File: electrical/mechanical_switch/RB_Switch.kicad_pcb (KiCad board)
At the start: 4 copper layers, 115 x 38 mm, 33 parts, among them SW1 SW_TH_Tactile_Omron_B3F-10xx, SW2 SW_TH_Tactile_Omron_B3F-10xx, SW3 SW_TH_Tactile_Omron_B3F-10xx, U1 ESP32-S2-MINI-1

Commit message: Address DRC shorts and minimum-clearance congestion
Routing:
- net USB_CC2: track 47.3 -> 43.2 mm, vias 2 -> 1
- net USB_DP: track 85.4 -> 84.8 mm, vias 3 -> 1
- net USB_DM: track 86.1 -> 85.6 mm, vias 3 -> 1
- net USB_CC1: vias 2 -> 1
- net VBAT: vias 6 -> 5
- net GND: vias 54 -> 44

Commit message: Re-route crowded PCB signal corridors and regulator connections
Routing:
- net SW1_NET: track 105.3 -> 103.3 mm
- net USB_DP: track 84.8 -> 83.1 mm
- net USB_DM: track 85.6 -> 83.8 mm, vias 1 -> 0
- net SW2_NET: track 96.3 -> 95.0 mm
- net USB_CC1: track 45.8 -> 45.0 mm
- net VBAT: vias 5 -> 4
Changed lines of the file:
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@@
-	)
-	(segment
-		(start 87.75 97.75)
-		(end 87 97.75)
-		(width 0.2)
-		(layer "In1.Cu")
-		(net "USB_CC1")
 	)
 	(segment
@@
 	)
 	(via
-		(at 105.4 87)
-		(size 0.5)
-		(drill 0.3)
-		(layers "F.Cu" "B.Cu")
-		(covering
-			(front no)
-			(back no)
-		)
-		(net "VBAT")
-	)
-	(via
 		(at 121.225 86)
 		(size 0.5)
@@
 	)
 	(segment
-		(start 124.75 99)
-		(end 124.75 99.5)
-		(width 0.2)
-		(layer "In2.Cu")
-		(net "SW1_NET")
-	)
-	(segment
 		(start 156.25 100.25)
 		(end 156.25 104)
@@
 	)
 	(segment
-		(start 125.5 100)
-		(end 125.5 100.25)
-		(width 0.2)
-		(layer "In2.Cu")
-		(net "SW1_NET")
-	)
-	(segment
-		(start 124.75 99.5)
-		(end 125 99.5)
-		(width 0.2)
-		(layer "In2.Cu")
-		(net "SW1_NET")
-	)
-	(segment
 		(start 156.5 104.5)
 		(end 157 104.5)
@@
 	)
 	(segment
-		(start 125 100)
-		(end 125.5 100)
-		(width 0.2)
-		(layer "In2.Cu")
-		(net "SW1_NET")
-	)
-	(segment
 		(start 165.5 112.25)
 		(end 171.25 112.25)
@@
 	)
 	(segment
-		(start 125 99.5)
-		(end 125 100)
-		(width 0.2)
-		(layer "In2.Cu")
-		(net "SW1_NET")
-	)
-	(segment
 		(start 165.5 112.5)
 		(end 165.5 112.25)
@@
 	)
 	(segment
-		(start 150 98.5)
-		(end 150 98)
-		(width 0.2)
-		(layer "In2.Cu")
-		(net "SW2_NET")
-	)
-	(segment
 		(start 163.225 113)
 		(end 164.25 113)
@@
 	)
 	(segment
-		(start 149.75 99)
-		(end 149.75 98.5)
-		(width 0.2)
-		(layer "In2.Cu")
-		(net "SW2_NET")
-	)
-	(segment
 		(start 172 92.5)
 		(end 171.75 92.5)
@@
 		(net "SW2_NET")
 	)
-	(segment
-		(start 149.75 98.5)
-		(end 150 98.5)
-		(width 0.2)
-		(layer "In2.Cu")
-		(net "SW2_NET")
-	)
 	(via
 		(at 169.45 93.05)
@@
 		(net "SW3_NET")
 	)
-	(via
-		(at 169.45 99)
-		(size 0.5)
-		(drill 0.3)
-		(layers "F.Cu" "B.Cu")
-		(covering
-			(front no)
-			(back no)
-		)
-		(net "USB_DM")
-	)
-	(segment
-		(start 99.75 98.75)
-		(end 99.75 98.5)
-		(width 0.2)
-		(layer "In1.Cu")
-		(net "USB_DM")
-	)
-	(segment
-		(start 100 98)
-		(end 100.5 98)
-		(width 0.2)
-		(layer "In1.Cu")
-		(net "USB_DM")
-	)
 	(segment
 		(start 88.25 98.75)
@@
 	)
 	(segment
-		(start 100.5 98)
-		(end 100.5 97.75)
-		(width 0.2)
-		(layer "In1.Cu")
-		(net "USB_DM")
-	)
-	(segment
 		(start 87.68 98.75)
 		(end 99.75 98.75)
@@
 	)
 	(segment
-		(start 99.75 98.5)
-		(end 100 98.5)
-		(width 0.2)
-		(layer "In1.Cu")
-		(net "USB_DM")
-	)
-	(segment
-		(start 100 98.5)
-		(end 100 98)
-		(width 0.2)
-		(layer "In1.Cu")
-		(net "USB_DM")
-	)
-	(segment
 		(start 169.5 97.75)
 		(end 169.5 99)
@@
 	)
 	(segment
-		(start 99.75 99.5)
-		(end 100 99.5)
-		(width 0.2)
-		(layer "B.Cu")
-		(net "USB_DP")
-	)
-	(segment
 		(start 87.68 99.25)
 		(end 99.75 99.25)
@@
 	)
 	(segment
-		(start 99.75 99.25)
-		(end 99.75 99.5)
-		(width 0.2)
-		(layer "B.Cu")
-		(net "USB_DP")
-	)
-	(segment
-		(start 100 99.5)
-		(end 100 100)
-		(width 0.2)
-		(layer "B.Cu")
-		(net "USB_DP")
-	)
-	(segment
-		(start 100.5 100)
-		(end 100.5 100.25)
-		(width 0.2)
-		(layer "B.Cu")
-		(net "USB_DP")
-	)
-	(segment
 		(start 88.25 99.25)
 		(end 87.75 99.25)
@@
 		(start 88.25 98.25)
 		(end 88.25 99.25)
-		(width 0.2)
-		(layer "B.Cu")
-		(net "USB_DP")
-	)
-	(segment
-		(start 100 100)
-		(end 100.5 100)
 		(width 0.2)
 		(layer "B.Cu")
@@
 		(layer "B.Cu")
 		(net "L_A")
-	)
+	)\n\t(segment\n\t\t(start 87.68 97.75)\n\t\t(end 87.75 97.75)\n\t\t(width 0.2)\n\t\t(layer "In1.Cu")\n\t\t(net "USB_CC1")\n\t\t\n\t)\n\t(segment\n\t\t(start 99.75 99.25)\n\t\t(end 99.75 100.25)\n\t\t(width 0.2)\n\t\t(layer "B.Cu")\n\t\t(net "USB_DP")\n\t\t\n\t)\n\t(segment\n\t\t(start 99.75 100.25)\n\t\t(end 100.5 100.25)\n\t\t(width 0.2)\n\t\t(layer "B.Cu")\n\t\t(net "USB_DP")\n\t\t\n\t)\n\t(segment\n\t\t(start 99.75 98.75)\n\t\t(end 99.75 97.75)\n\t\t(width 0.2)\n\t\t(layer "In1.Cu")\n\t\t(net "USB_DM")\n\t\t\n\t)\n\t(segment\n\t\t(start 99.75 97.75)\n\t\t(end 100.5 97.75)\n\t\t(width 0.2)\n\t\t(layer "In1.Cu")\n\t\t(net "USB_DM")\n\t\t\n\t)\n\t(segment\n\t\t(start 124.75 99)\n\t\t(end 124.75 101)\n\t\t(width 0.2)\n\t\t(layer "In2.Cu")\n\t\t(net "SW1_NET")\n\t\t\n\t)\n\t(segment\n\t\t(start 124.75 101)\n\t\t(end 125.5 101)\n\t\t(width 0.2)\n\t\t(layer "In2.Cu")\n\t\t(net "SW1_NET")\n\t\t\n\t)\n\t(segment\n\t\t(start 125.5 101)\n\t\t(end 125.5 100.25)\n\t\t(width 0.2)\n\t\t(layer "In2.Cu")\n\t\t(net "SW1_NET")\n\t\t\n\t)\n\t(segment\n\t\t(start 149.75 99)\n\t\t(end 149.75 97.75)\n\t\t(width 0.2)\n\t\t(layer "In2.Cu")\n\t\t(net "SW2_NET")\n\t\t\n\t)\n\t(segment\n\t\t(start 149.75 97.75)\n\t\t(end 150.5 97.75)\n\t\t(width 0.2)\n\t\t(layer "In2.Cu")\n\t\t(net "SW2_NET")\n\t\t\n\t)\n\t(segment\n\t\t(start 150.5 97.75)\n\t\t(end 150.5 98)\n\t\t(width 0.2)\n\t\t(layer "In2.Cu")\n\t\t(net "SW2_NET")\n\t\t\n\t)\n\t(segment\n\t\t(start 150.5 98)\n\t\t(end 150 98)\n\t\t(width 0.2)\n\t\t(layer "In2.Cu")\n\t\t(net "SW2_NET")\n\t\t\n\t)\n\t(segment\n\t\t(start 102.6 85.5)\n\t\t(end 101 84.5)\n\t\t(width 0.2)\n\t\t(layer "F.Cu")\n\t\t(net "L_B")\n\t\t\n\t)\n\t(segment\n\t\t(start 102.6 86.5)\n\t\t(end 101 87.5)\n\t\t(width 0.2)\n\t\t(layer "F.Cu")\n\t\t(net "L_A")\n\t\t\n\t)\n\t(segment\n\t\t(start 102.6 85)\n\t\t(end 101 83.5)\n\t\t(width 0.2)\n\t\t(layer "F.Cu")\n\t\t(net "V3V3")\n\t\t\n\t)\n\t(segment\n\t\t(start 102.6 87)\n\t\t(end 103.5 88.5)\n\t\t(width 0.2)\n\t\t(layer "F.Cu")\n\t\t(net "VBAT")\n\t\t\n\t)\n\t(segment\n\t\t(start 102.6 86)\n\t\t(end 103.425 86)\n\t\t(width 0.2)\n\t\t(layer "F.Cu")\n\t\t(net "GND")\n\t\t\n\t)\n\t(segment\n\t\t(start 105.4 85.5)\n\t\t(end 104.575 86)\n\t\t(width 0.2)\n\t\t(layer "F.Cu")\n\t\t(net "GND")\n\t\t\n\t)\n\t(segment\n\t\t(start 105.4 86.5)\n\t\t(end 104.575 86)\n\t\t(width 0.2)\n\t\t(layer "F.Cu")\n\t\t(net "GND")\n\t\t\n\t)\n\t(segment\n\t\t(start 87.68 100.75)\n\t\t(end 88.25 100.75)\n\t\t(width 0.2)\n\t\t(layer "F.Cu")\n\t\t(net "USB_CC2")\n\t\t\n\t)

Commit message: Repair PCB routing changes and keep board syntax valid
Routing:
- net SW1_NET: track 103.3 -> 106.8 mm
- net GND: track 0.00 -> 2.75 mm
- net SW2_NET: track 95.0 -> 97.8 mm
- net V3V3: track 0.00 -> 2.19 mm
- net L_B: track 5.00 -> 6.89 mm
- net L_A: track 5.00 -> 6.89 mm
- net USB_DP: track 83.1 -> 84.8 mm
- net USB_DM: track 83.8 -> 85.6 mm
- net VBAT: track 73.6 -> 75.4 mm
- net USB_CC2: track 43.2 -> 43.8 mm
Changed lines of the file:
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@@
 	)
 	(embedded_fonts no)
-)
-	(via
-		(at 90 97)
-		(size 0.5)
-		(drill 0.3)
-		(layers "F.Cu" "B.Cu")
-		(net "USB_CC1")
-	)
-	(via
-		(at 90 98)
-		(size 0.5)
-		(drill 0.3)
-		(layers "F.Cu" "B.Cu")
-		(net "USB_DP")
-	)
-	(via
-		(at 90 99)
-		(size 0.5)
-		(drill 0.3)
-		(layers "F.Cu" "B.Cu")
-		(net "USB_DP")
-	)
-	(via
-		(at 91 98.5)
-		(size 0.5)
-		(drill 0.3)
-		(layers "F.Cu" "B.Cu")
-		(net "USB_DM")
-	)
-	(via
-		(at 91 99.5)
-		(size 0.5)
-		(drill 0.3)
-		(layers "F.Cu" "B.Cu")
-		(net "USB_DM")
-	)
-	(via
-		(at 91 100.5)
-		(size 0.5)
-		(drill 0.3)
-		(layers "F.Cu" "B.Cu")
-		(net "USB_CC2")
-	)
 	(segment
-		(start 90 97)
+		(start 87.68 97.75)
 		(end 87.75 97.75)
 		(width 0.2)
@@
 	)
 	(segment
-		(start 90 98)
-		(end 88.25 98.25)
+		(start 99.75 99.25)
+		(end 99.75 100.25)
 		(width 0.2)
 		(layer "B.Cu")
@@
 	)
 	(segment
-		(start 90 99)
-		(end 88.25 99.25)
+		(start 99.75 100.25)
+		(end 100.5 100.25)
 		(width 0.2)
 		(layer "B.Cu")
@@
 	)
 	(segment
-		(start 91 98.5)
-		(end 88.25 98.75)
+		(start 99.75 98.75)
+		(end 99.75 97.75)
 		(width 0.2)
 		(layer "In1.Cu")
@@
 	)
 	(segment
-		(start 91 99.5)
-		(end 88.25 99.75)
+		(start 99.75 97.75)
+		(end 100.5 97.75)
 		(width 0.2)
 		(layer "In1.Cu")
@@
 	)
 	(segment
-		(start 91 100.5)
-		(end 91.75 100.75)
+		(start 124.75 99)
+		(end 124.75 101)
 		(width 0.2)
-		(layer "B.Cu")
-		(net "USB_CC2")
+		(layer "In2.Cu")
+		(net "SW1_NET")
 	)
 	(segment
-		(start 101 84.5)
-		(end 101 85.25)
+		(start 124.75 101)
+		(end 125.5 101)
 		(width 0.2)
-		(layer "B.Cu")
+		(layer "In2.Cu")
+		(net "SW1_NET")
+	)
+	(segment
+		(start 125.5 101)
+		(end 125.5 100.25)
+		(width 0.2)
+		(layer "In2.Cu")
+		(net "SW1_NET")
+	)
+	(segment
+		(start 149.75 99)
+		(end 149.75 97.75)
+		(width 0.2)
+		(layer "In2.Cu")
+		(net "SW2_NET")
+	)
+	(segment
+		(start 149.75 97.75)
+		(end 150.5 97.75)
+		(width 0.2)
+		(layer "In2.Cu")
+		(net "SW2_NET")
+	)
+	(segment
+		(start 150.5 97.75)
+		(end 150.5 98)
+		(width 0.2)
+		(layer "In2.Cu")
+		(net "SW2_NET")
+	)
+	(segment
+		(start 150.5 98)
+		(end 150 98)
+		(width 0.2)
+		(layer "In2.Cu")
+		(net "SW2_NET")
+	)
+	(segment
+		(start 102.6 85.5)
+		(end 101 84.5)
+		(width 0.2)
+		(layer "F.Cu")
 		(net "L_B")
 	)
 	(segment
-		(start 101 84.5)
-		(end 98.5 84.5)
+		(start 102.6 86.5)
+		(end 101 87.5)
 		(width 0.2)
-		(layer "B.Cu")
-		(net "L_B")
-	)
-	(segment
-		(start 101 87.5)
-		(end 102 87.5)
-		(width 0.2)
-		(layer "B.Cu")
+		(layer "F.Cu")
 		(net "L_A")
 	)
 	(segment
-		(start 101 87.5)
-		(end 98.5 87.5)
-		(width 0.2)
-		(layer "B.Cu")
-		(net "L_A")
-	)
-	(segment
-		(start 101 83.5)
-		(end 102.6 85)
+		(start 102.6 85)
+		(end 101 83.5)
 		(width 0.2)
 		(layer "F.Cu")
@@
 	)
 	(segment
-		(start 103.5 88.5)
-		(end 103.5 87.5)
+		(start 102.6 87)
+		(end 103.5 88.5)
 		(width 0.2)
-		(layer "B.Cu")
+		(layer "F.Cu")
 		(net "VBAT")
 	)
 	(segment
-		(start 98.6 83.725)
-		(end 98.5 84.5)
+		(start 102.6 86)
+		(end 103.425 86)
 		(width 0.2)
-		(layer "B.Cu")
-		(net "L_B")
+		(layer "F.Cu")
+		(net "GND")
 	)
 	(segment
-		(start 98.6 88.275)
-		(end 98.5 87.5)
+		(start 105.4 85.5)
+		(end 104.575 86)
 		(width 0.2)
-		(layer "B.Cu")
-		(net "L_A")
-	)\n\t(segment\n\t\t(start 87.68 97.75)\n\t\t(end 87.75 97.75)\n\t\t(width 0.2)\n\t\t(layer "In1.Cu")\n\t\t(net "USB_CC1")\n\t\t\n\t)\n\t(segment\n\t\t(start 99.75 99.25)\n\t\t(end 99.75 100.25)\n\t\t(width 0.2)\n\t\t(layer "B.Cu")\n\t\t(net "USB_DP")\n\t\t\n\t)\n\t(segment\n\t\t(start 99.75 100.25)\n\t\t(end 100.5 100.25)\n\t\t(width 0.2)\n\t\t(layer "B.Cu")\n\t\t(net "USB_DP")\n\t\t\n\t)\n\t(segment\n\t\t(start 99.75 98.75)\n\t\t(end 99.75 97.75)\n\t\t(width 0.2)\n\t\t(layer "In1.Cu")\n\t\t(net "USB_DM")\n\t\t\n\t)\n\t(segment\n\t\t(start 99.75 97.75)\n\t\t(end 100.5 97.75)\n\t\t(width 0.2)\n\t\t(layer "In1.Cu")\n\t\t(net "USB_DM")\n\t\t\n\t)\n\t(segment\n\t\t(start 124.75 99)\n\t\t(end 124.75 101)\n\t\t(width 0.2)\n\t\t(layer "In2.Cu")\n\t\t(net "SW1_NET")\n\t\t\n\t)\n\t(segment\n\t\t(start 124.75 101)\n\t\t(end 125.5 101)\n\t\t(width 0.2)\n\t\t(layer "In2.Cu")\n\t\t(net "SW1_NET")\n\t\t\n\t)\n\t(segment\n\t\t(start 125.5 101)\n\t\t(end 125.5 100.25)\n\t\t(width 0.2)\n\t\t(layer "In2.Cu")\n\t\t(net "SW1_NET")\n\t\t\n\t)\n\t(segment\n\t\t(start 149.75 99)\n\t\t(end 149.75 97.75)\n\t\t(width 0.2)\n\t\t(layer "In2.Cu")\n\t\t(net "SW2_NET")\n\t\t\n\t)\n\t(segment\n\t\t(start 149.75 97.75)\n\t\t(end 150.5 97.75)\n\t\t(width 0.2)\n\t\t(layer "In2.Cu")\n\t\t(net "SW2_NET")\n\t\t\n\t)\n\t(segment\n\t\t(start 150.5 97.75)\n\t\t(end 150.5 98)\n\t\t(width 0.2)\n\t\t(layer "In2.Cu")\n\t\t(net "SW2_NET")\n\t\t\n\t)\n\t(segment\n\t\t(start 150.5 98)\n\t\t(end 150 98)\n\t\t(width 0.2)\n\t\t(layer "In2.Cu")\n\t\t(net "SW2_NET")\n\t\t\n\t)\n\t(segment\n\t\t(start 102.6 85.5)\n\t\t(end 101 84.5)\n\t\t(width 0.2)\n\t\t(layer "F.Cu")\n\t\t(net "L_B")\n\t\t\n\t)\n\t(segment\n\t\t(start 102.6 86.5)\n\t\t(end 101 87.5)\n\t\t(width 0.2)\n\t\t(layer "F.Cu")\n\t\t(net "L_A")\n\t\t\n\t)\n\t(segment\n\t\t(start 102.6 85)\n\t\t(end 101 83.5)\n\t\t(width 0.2)\n\t\t(layer "F.Cu")\n\t\t(net "V3V3")\n\t\t\n\t)\n\t(segment\n\t\t(start 102.6 87)\n\t\t(end 103.5 88.5)\n\t\t(width 0.2)\n\t\t(layer "F.Cu")\n\t\t(net "VBAT")\n\t\t\n\t)\n\t(segment\n\t\t(start 102.6 86)\n\t\t(end 103.425 86)\n\t\t(width 0.2)\n\t\t(layer "F.Cu")\n\t\t(net "GND")\n\t\t\n\t)\n\t(segment\n\t\t(start 105.4 85.5)\n\t\t(end 104.575 86)\n\t\t(width 0.2)\n\t\t(layer "F.Cu")\n\t\t(net "GND")\n\t\t\n\t)\n\t(segment\n\t\t(start 105.4 86.5)\n\t\t(end 104.575 86)\n\t\t(width 0.2)\n\t\t(layer "F.Cu")\n\t\t(net "GND")\n\t\t\n\t)\n\t(segment\n\t\t(start 87.68 100.75)\n\t\t(end 88.25 100.75)\n\t\t(width 0.2)\n\t\t(layer "F.Cu")\n\t\t(net "USB_CC2")\n\t\t\n\t)
+		(layer "F.Cu")
+		(net "GND")
+	)
+	(segment
+		(start 105.4 86.5)
+		(end 104.575 86)
+		(width 0.2)
+		(layer "F.Cu")
+		(net "GND")
+	)
+	(segment
+		(start 87.68 100.75)
+		(end 88.25 100.75)
+		(width 0.2)
+		(layer "F.Cu")
+		(net "USB_CC2")
+	)
+)

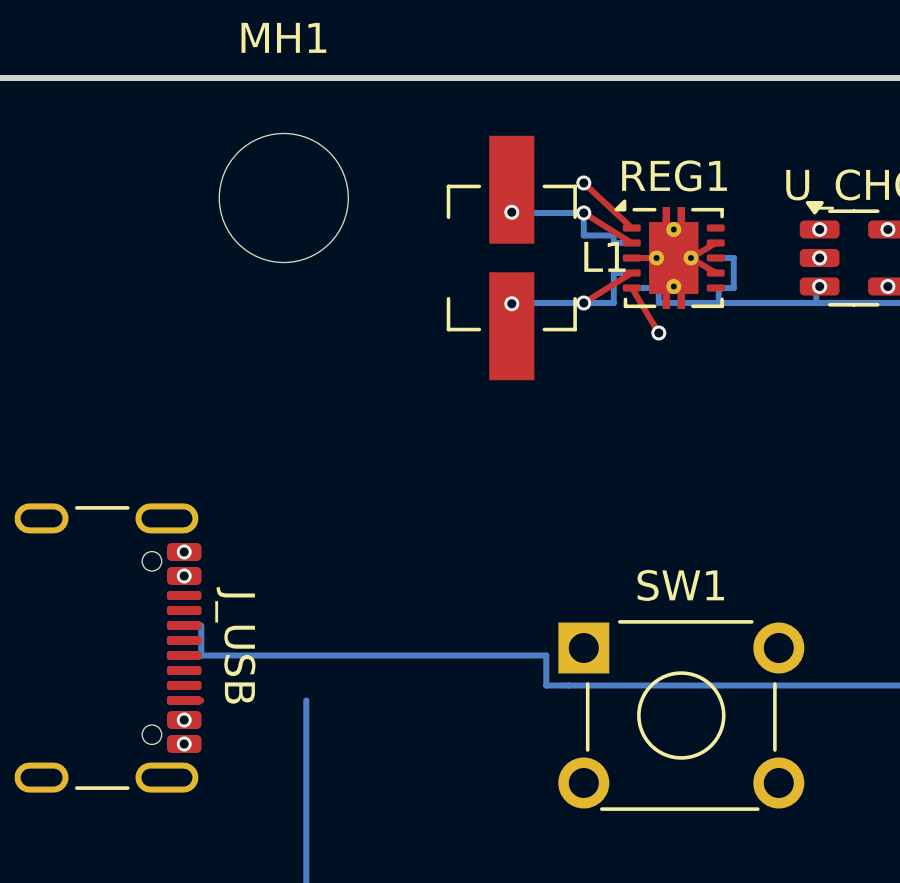
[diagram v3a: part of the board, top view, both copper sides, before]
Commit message: Resolve remaining PCB proximity hotspots and regulator connectivity
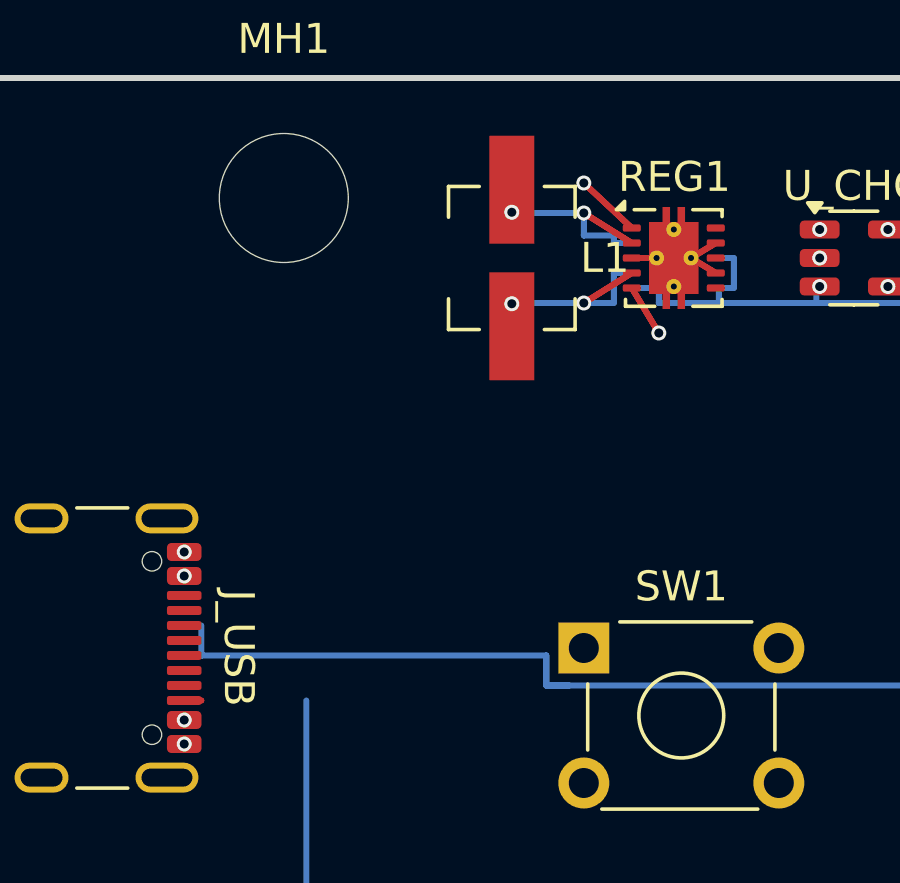
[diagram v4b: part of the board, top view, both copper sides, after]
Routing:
- net SW1_NET: track 106.8 -> 110.3 mm
- net GND: track 2.75 -> 5.51 mm
- net SW2_NET: track 97.8 -> 100.5 mm
- net V3V3: track 2.19 -> 4.39 mm
- net L_B: track 6.89 -> 8.77 mm
- net L_A: track 6.89 -> 8.77 mm
- net USB_DP: track 84.8 -> 86.6 mm
- net USB_DM: track 85.6 -> 87.3 mm
- net VBAT: track 75.4 -> 77.1 mm
- net USB_CC2: track 43.8 -> 44.4 mm
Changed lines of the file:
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@@
+		(net "USB_CC2")
+	)
+	(segment
+		(start 87.68 97.75)
+		(end 87.75 97.75)
+		(width 0.2)
+		(layer "In1.Cu")
+		(net "USB_CC1")
+	)
+	(segment
+		(start 99.75 99.25)
+		(end 99.75 100.25)
+		(width 0.2)
+		(layer "B.Cu")
+		(net "USB_DP")
+	)
+	(segment
+		(start 99.75 100.25)
+		(end 100.5 100.25)
+		(width 0.2)
+		(layer "B.Cu")
+		(net "USB_DP")
+	)
+	(segment
+		(start 99.75 98.75)
+		(end 99.75 97.75)
+		(width 0.2)
+		(layer "In1.Cu")
+		(net "USB_DM")
+	)
+	(segment
+		(start 99.75 97.75)
+		(end 100.5 97.75)
+		(width 0.2)
+		(layer "In1.Cu")
+		(net "USB_DM")
+	)
+	(segment
+		(start 124.75 99)
+		(end 124.75 101)
+		(width 0.2)
+		(layer "In2.Cu")
+		(net "SW1_NET")
+	)
+	(segment
+		(start 124.75 101)
+		(end 125.5 101)
+		(width 0.2)
+		(layer "In2.Cu")
+		(net "SW1_NET")
+	)
+	(segment
+		(start 125.5 101)
+		(end 125.5 100.25)
+		(width 0.2)
+		(layer "In2.Cu")
+		(net "SW1_NET")
+	)
+	(segment
+		(start 149.75 99)
+		(end 149.75 97.75)
+		(width 0.2)
+		(layer "In2.Cu")
+		(net "SW2_NET")
+	)
+	(segment
+		(start 149.75 97.75)
+		(end 150.5 97.75)
+		(width 0.2)
+		(layer "In2.Cu")
+		(net "SW2_NET")
+	)
+	(segment
+		(start 150.5 97.75)
+		(end 150.5 98)
+		(width 0.2)
+		(layer "In2.Cu")
+		(net "SW2_NET")
+	)
+	(segment
+		(start 150.5 98)
+		(end 150 98)
+		(width 0.2)
+		(layer "In2.Cu")
+		(net "SW2_NET")
+	)
+	(segment
+		(start 102.6 85.5)
+		(end 101 84.5)
+		(width 0.2)
+		(layer "F.Cu")
+		(net "L_B")
+	)
+	(segment
+		(start 102.6 86.5)
+		(end 101 87.5)
+		(width 0.2)
+		(layer "F.Cu")
+		(net "L_A")
+	)
+	(segment
+		(start 102.6 85)
+		(end 101 83.5)
+		(width 0.2)
+		(layer "F.Cu")
+		(net "V3V3")
+	)
+	(segment
+		(start 102.6 87)
+		(end 103.5 88.5)
+		(width 0.2)
+		(layer "F.Cu")
+		(net "VBAT")
+	)
+	(segment
+		(start 102.6 86)
+		(end 103.425 86)
+		(width 0.2)
+		(layer "F.Cu")
+		(net "GND")
+	)
+	(segment
+		(start 105.4 85.5)
+		(end 104.575 86)
+		(width 0.2)
+		(layer "F.Cu")
+		(net "GND")
+	)
+	(segment
+		(start 105.4 86.5)
+		(end 104.575 86)
+		(width 0.2)
+		(layer "F.Cu")
+		(net "GND")
+	)
+	(segment
+		(start 87.68 100.75)
+		(end 88.25 100.75)
+		(width 0.2)
+		(layer "F.Cu")
 		(net "USB_CC2")
 	)
